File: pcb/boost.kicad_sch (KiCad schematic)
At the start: 9 parts, among them U1 LM2733XMF

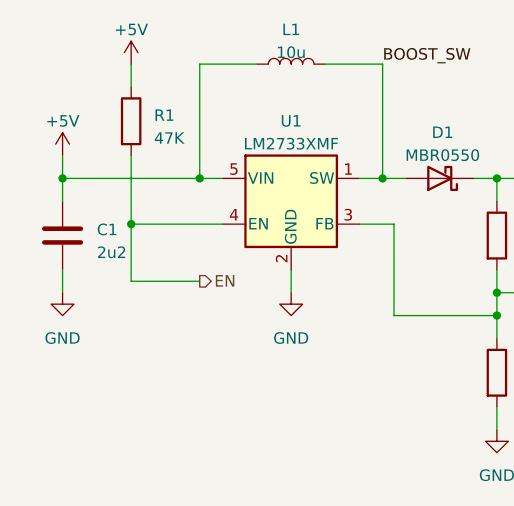
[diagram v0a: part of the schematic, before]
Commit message: * Work in progress
  - Add generate script
  - Add switch model
  - Start routing
  - Tidy schematic
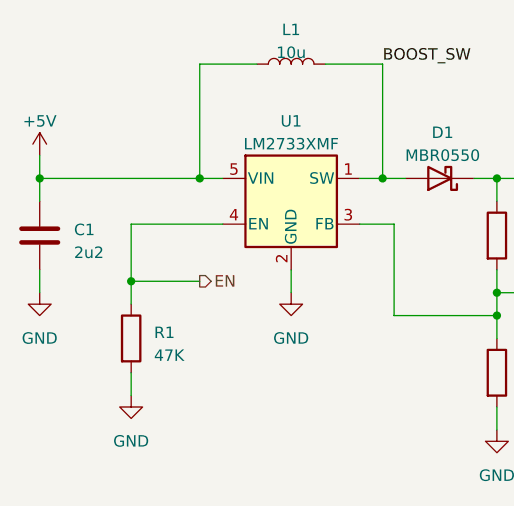
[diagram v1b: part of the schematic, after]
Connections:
- net +5V: no longer R1.1
- net EN: now also R1.1; no longer R1.2
- net GND: now also R1.2
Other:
- moved on the sheet: C1, R1
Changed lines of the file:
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@@
   (junction (at 134.62 82.55) (diameter 0) (color 0 0 0 0)
   )
-  (junction (at 106.68 87.63) (diameter 0) (color 0 0 0 0)
-  )
-  (junction (at 99.06 82.55) (diameter 0) (color 0 0 0 0)
+  (junction (at 96.52 82.55) (diameter 0) (color 0 0 0 0)
   )
   (junction (at 147.32 97.79) (diameter 0) (color 0 0 0 0)
@@
   (junction (at 156.21 82.55) (diameter 0) (color 0 0 0 0)
   )
+  (junction (at 106.68 93.98) (diameter 0) (color 0 0 0 0)
+  )
   (wire (pts (xy 147.32 95.25) (xy 147.32 97.79))
     (stroke (width 0) (type default))
@@
     (stroke (width 0) (type default))
   )
-  (wire (pts (xy 99.06 80.01) (xy 99.06 82.55))
+  (wire (pts (xy 96.52 80.01) (xy 96.52 82.55))
     (stroke (width 0) (type default))
   )
@@
     (stroke (width 0) (type default))
   )
-  (wire (pts (xy 106.68 69.85) (xy 106.68 72.39))
-    (stroke (width 0) (type default))
-  )
   (wire (pts (xy 134.62 69.85) (xy 134.62 82.55))
     (stroke (width 0) (type default))
@@
     (stroke (width 0) (type default))
   )
+  (wire (pts (xy 106.68 93.98) (xy 106.68 96.52))
+    (stroke (width 0) (type default))
+  )
   (wire (pts (xy 167.64 92.71) (xy 167.64 95.25))
     (stroke (width 0) (type default))
@@
     (stroke (width 0) (type default))
   )
-  (wire (pts (xy 106.68 87.63) (xy 106.68 80.01))
-    (stroke (width 0) (type default))
-  )
   (wire (pts (xy 135.89 87.63) (xy 135.89 97.79))
     (stroke (width 0) (type default))
   )
-  (wire (pts (xy 99.06 82.55) (xy 114.3 82.55))
+  (wire (pts (xy 96.52 82.55) (xy 114.3 82.55))
     (stroke (width 0) (type default))
   )
@@
     (stroke (width 0) (type default))
   )
-  (wire (pts (xy 99.06 85.09) (xy 99.06 82.55))
+  (wire (pts (xy 96.52 85.09) (xy 96.52 82.55))
     (stroke (width 0) (type default))
   )
@@
     (stroke (width 0) (type default))
   )
-  (wire (pts (xy 99.06 92.71) (xy 99.06 95.25))
+  (wire (pts (xy 96.52 92.71) (xy 96.52 95.25))
     (stroke (width 0) (type default))
   )
@@
   )
   (wire (pts (xy 167.64 82.55) (xy 156.21 82.55))
+    (stroke (width 0) (type default))
+  )
+  (wire (pts (xy 106.68 104.14) (xy 106.68 106.68))
     (stroke (width 0) (type default))
   )
@@
     )
   )
-  (symbol (lib_id "power:+5V") (at 106.68 69.85 0) (unit 1)
-    (in_bom yes) (on_board yes) (dnp no) (fields_autoplaced)
-    (property "Reference" "#PWR03" (at 106.68 73.66 0)
-      (effects (font (size 1.27 1.27)) hide)
-    )
-    (property "Value" "+5V" (at 106.68 66.04 0)
-      (effects (font (size 1.27 1.27)))
-    )
-    (property "Footprint" "" (at 106.68 69.85 0)
-      (effects (font (size 1.27 1.27)) hide)
-    )
-    (property "Datasheet" "" (at 106.68 69.85 0)
-      (effects (font (size 1.27 1.27)) hide)
-    )
-    (pin "1")
-    (instances
-      (project "mbus-reader-proto"
-        (path "/36d146b0-f348-4341-a935-471af0e684a6"
-          (reference "#PWR03") (unit 1)
-        )
-        (path "/36d146b0-f348-4341-a935-471af0e684a6/d9d13df7-ec5a-4d9a-8998-14ae0ed59560"
-          (reference "#PWR04") (unit 1)
-        )
-      )
-      (project "emonHP"
-        (path "/afefbb79-c2cc-4097-b792-3e37a295b6e5/d4153821-464a-43cf-949b-6df0813cc359"
-          (reference "#PWR025") (unit 1)
-        )
-      )
-    )
-  )
   (symbol (lib_id "Device:C") (at 156.21 88.9 0) (unit 1)
     (in_bom yes) (on_board yes) (dnp no) (fields_autoplaced)
@@
     )
   )
-  (symbol (lib_id "Device:R") (at 106.68 76.2 0) (unit 1)
-    (in_bom yes) (on_board yes) (dnp no) (fields_autoplaced)
-    (property "Reference" "R1" (at 109.22 75.565 0)
-      (effects (font (size 1.27 1.27)) (justify left))
-    )
-    (property "Value" "47K" (at 109.22 78.105 0)
-      (effects (font (size 1.27 1.27)) (justify left))
-    )
-    (property "Footprint" "Resistor_SMD:R_0402_1005Metric" (at 104.902 76.2 90)
-      (effects (font (size 1.27 1.27)) hide)
-    )
-    (property "Datasheet" "~" (at 106.68 76.2 0)
+  (symbol (lib_id "Device:R") (at 106.68 100.33 0) (unit 1)
+    (in_bom yes) (on_board yes) (dnp no) (fields_autoplaced)
+    (property "Reference" "R1" (at 109.22 99.695 0)
+      (effects (font (size 1.27 1.27)) (justify left))
+    )
+    (property "Value" "47K" (at 109.22 102.235 0)
+      (effects (font (size 1.27 1.27)) (justify left))
+    )
+    (property "Footprint" "Resistor_SMD:R_0402_1005Metric" (at 104.902 100.33 90)
+      (effects (font (size 1.27 1.27)) hide)
+    )
+    (property "Datasheet" "~" (at 106.68 100.33 0)
       (effects (font (size 1.27 1.27)) hide)
     )
@@
     )
   )
-  (symbol (lib_id "Device:C") (at 99.06 88.9 0) (unit 1)
-    (in_bom yes) (on_board yes) (dnp no) (fields_autoplaced)
-    (property "Reference" "C1" (at 102.87 88.265 0)
-      (effects (font (size 1.27 1.27)) (justify left))
-    )
-    (property "Value" "2u2" (at 102.87 90.805 0)
-      (effects (font (size 1.27 1.27)) (justify left))
-    )
-    (property "Footprint" "Capacitor_SMD:C_0603_1608Metric" (at 100.0252 92.71 0)
-      (effects (font (size 1.27 1.27)) hide)
-    )
-    (property "Datasheet" "~" (at 99.06 88.9 0)
+  (symbol (lib_id "power:GND") (at 106.68 106.68 0) (unit 1)
+    (in_bom yes) (on_board yes) (dnp no) (fields_autoplaced)
+    (property "Reference" "#PWR02" (at 106.68 113.03 0)
+      (effects (font (size 1.27 1.27)) hide)
+    )
+    (property "Value" "GND" (at 106.68 111.76 0)
+      (effects (font (size 1.27 1.27)))
+    )
+    (property "Footprint" "" (at 106.68 106.68 0)
+      (effects (font (size 1.27 1.27)) hide)
+    )
+    (property "Datasheet" "" (at 106.68 106.68 0)
+      (effects (font (size 1.27 1.27)) hide)
+    )
+    (pin "1")
+    (instances
+      (project "mbus-reader-proto"
+        (path "/36d146b0-f348-4341-a935-471af0e684a6"
+          (reference "#PWR02") (unit 1)
+        )
+        (path "/36d146b0-f348-4341-a935-471af0e684a6/d9d13df7-ec5a-4d9a-8998-14ae0ed59560"
+          (reference "#PWR05") (unit 1)
+        )
+      )
+      (project "emonHP"
+        (path "/afefbb79-c2cc-4097-b792-3e37a295b6e5/d4153821-464a-43cf-949b-6df0813cc359"
+          (reference "#PWR025") (unit 1)
+        )
+      )
+    )
+  )
+  (symbol (lib_id "Device:C") (at 96.52 88.9 0) (unit 1)
+    (in_bom yes) (on_board yes) (dnp no) (fields_autoplaced)
+    (property "Reference" "C1" (at 100.33 88.265 0)
+      (effects (font (size 1.27 1.27)) (justify left))
+    )
+    (property "Value" "2u2" (at 100.33 90.805 0)
+      (effects (font (size 1.27 1.27)) (justify left))
+    )
+    (property "Footprint" "Capacitor_SMD:C_0603_1608Metric" (at 97.4852 92.71 0)
+      (effects (font (size 1.27 1.27)) hide)
+    )
+    (property "Datasheet" "~" (at 96.52 88.9 0)
       (effects (font (size 1.27 1.27)) hide)
     )
@@
     )
   )
-  (symbol (lib_id "power:+5V") (at 99.06 80.01 0) (unit 1)
-    (in_bom yes) (on_board yes) (dnp no) (fields_autoplaced)
-    (property "Reference" "#PWR06" (at 99.06 83.82 0)
-      (effects (font (size 1.27 1.27)) hide)
-    )
-    (property "Value" "+5V" (at 99.06 76.2 0)
-      (effects (font (size 1.27 1.27)))
-    )
-    (property "Footprint" "" (at 99.06 80.01 0)
-      (effects (font (size 1.27 1.27)) hide)
-    )
-    (property "Datasheet" "" (at 99.06 80.01 0)
+  (symbol (lib_id "power:+5V") (at 96.52 80.01 0) (unit 1)
+    (in_bom yes) (on_board yes) (dnp no) (fields_autoplaced)
+    (property "Reference" "#PWR06" (at 96.52 83.82 0)
+      (effects (font (size 1.27 1.27)) hide)
+    )
+    (property "Value" "+5V" (at 96.52 76.2 0)
+      (effects (font (size 1.27 1.27)))
+    )
+    (property "Footprint" "" (at 96.52 80.01 0)
+      (effects (font (size 1.27 1.27)) hide)
+    )
+    (property "Datasheet" "" (at 96.52 80.01 0)
       (effects (font (size 1.27 1.27)) hide)
     )
@@
     )
   )
-  (symbol (lib_id "power:GND") (at 99.06 95.25 0) (unit 1)
-    (in_bom yes) (on_board yes) (dnp no) (fields_autoplaced)
-    (property "Reference" "#PWR05" (at 99.06 101.6 0)
-      (effects (font (size 1.27 1.27)) hide)
-    )
-    (property "Value" "GND" (at 99.06 100.33 0)
-      (effects (font (size 1.27 1.27)))
-    )
-    (property "Footprint" "" (at 99.06 95.25 0)
-      (effects (font (size 1.27 1.27)) hide)
-    )
-    (property "Datasheet" "" (at 99.06 95.25 0)
-      (effects (font (size 1.27 1.27)) hide)
-    )
+  (symbol (lib_id "power:GND") (at 96.52 95.25 0) (unit 1)
+    (in_bom yes) (on_board yes) (dnp no) (fields_autoplaced)
+    (property "Reference" "#PWR05" (at 96.52 101.6 0)
+      (effects (font (size 1.27 1.27)) hide)
+    )
+    (property "Value" "GND" (at 96.52 100.33 0)
+      (effects (font (size 1.27 1.27)))
+    )
+    (property "Footprint" "" (at 96.52 95.25 0)
+      (effects (font (size 1.27 1.27)) hide)
+    )
+    (property "Datasheet" "" (at 96.52 95.25 0)
+      (effects (font (size 1.27 1.27)) hide)
+    )

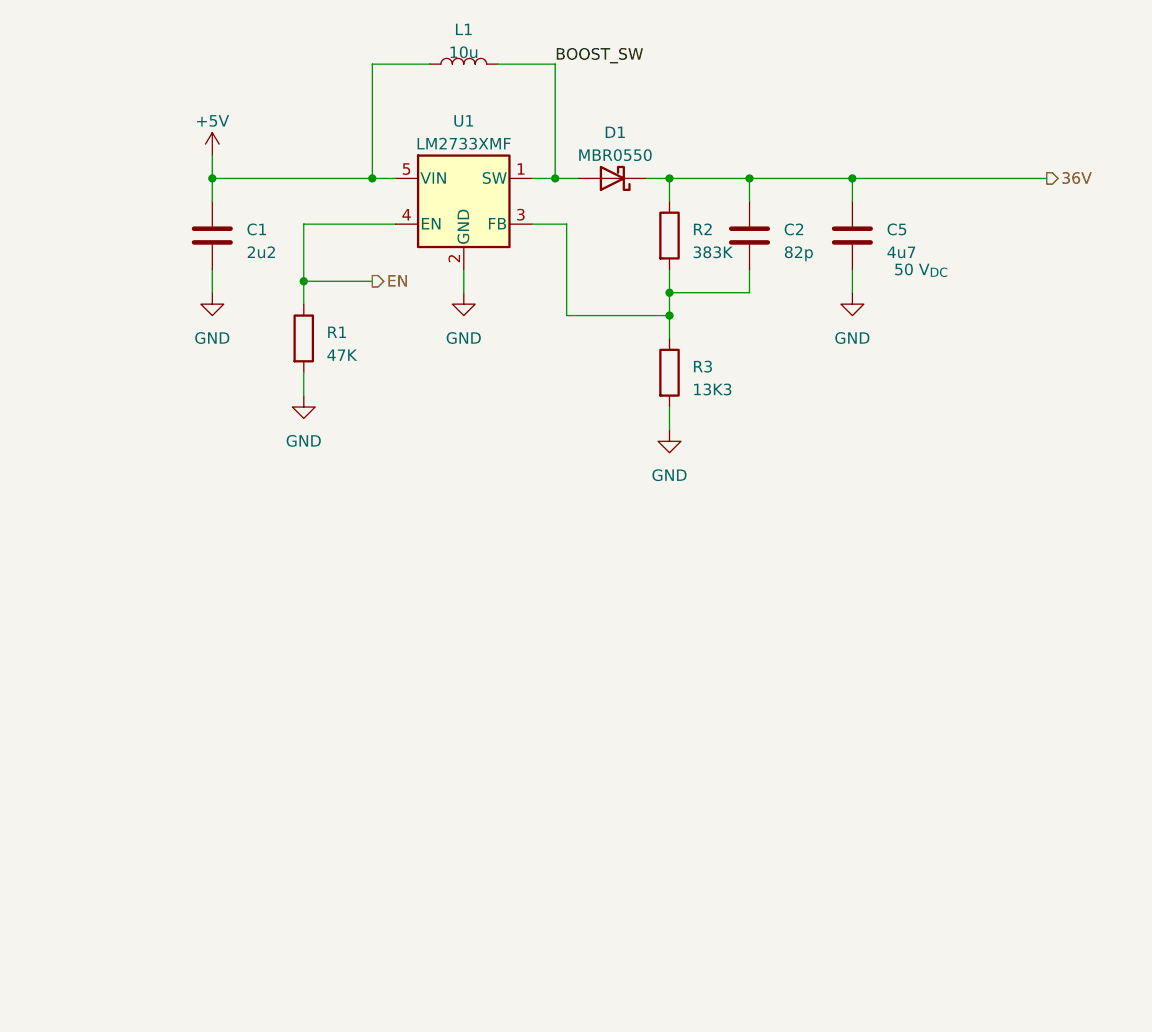
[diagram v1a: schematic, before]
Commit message: * [0.1-dev] Voltage good
  - Add 36V voltage good detection
  - Add all 3D models
  - Correct footprint for front LED
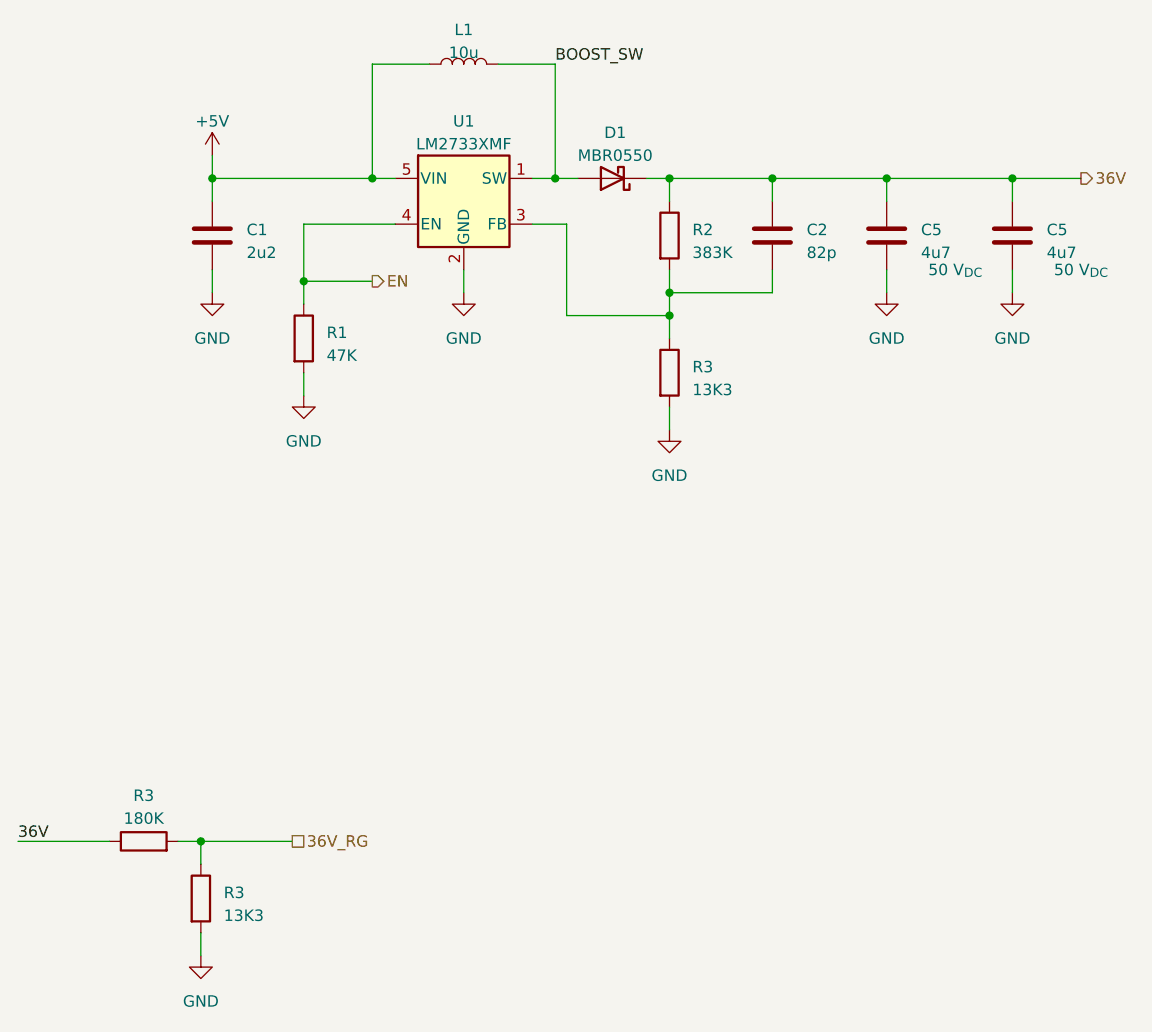
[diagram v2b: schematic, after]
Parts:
- added C5: 4u7, Capacitor_SMD:C_0805_2012Metric, symbol Device:C
- added R3: 180K, Resistor_SMD:R_0402_1005Metric, symbol Device:R
- added R3: 13K3, Resistor_SMD:R_0402_1005Metric, symbol Device:R
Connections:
- net +5V: now also L1.2; no longer L1.1
- net 36V: now also C5.1, R3.1
- net BOOST_SW: now also L1.1; no longer L1.2
- net GND: now also C5.2, R3.2
- new net 36V_RG: R3.1, R3.2
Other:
- moved on the sheet: C2, C5, L1

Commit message: [v0.1-dev] First pass on emonPi format
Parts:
- removed R3: 180K, Resistor_SMD:R_0402_1005Metric, symbol Device:R
- removed R3: 13K3, Resistor_SMD:R_0402_1005Metric, symbol Device:R
- L?: renamed from L1; MPN (none) -> ASPI-3012S-100M-T; Mouser (none) -> 815-ASPI-3012S-100MT
- U?: renamed from U1; MPN (none) -> LM2733XMFX/NOPB; Mouser (none) -> 926-LM2733XMFX/NOPB
- renumbered C2 to C?, C5 to C?, C1 to C?, D1 to D?, R3 to R?, R1 to R?, R2 to R?
